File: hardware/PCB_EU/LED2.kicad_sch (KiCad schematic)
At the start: 28 parts, among them J601 LED2 + / GND, J602 BAR2 + / GND, Q601 IRF540ZPBF, U601 LM3429MH/NOPB

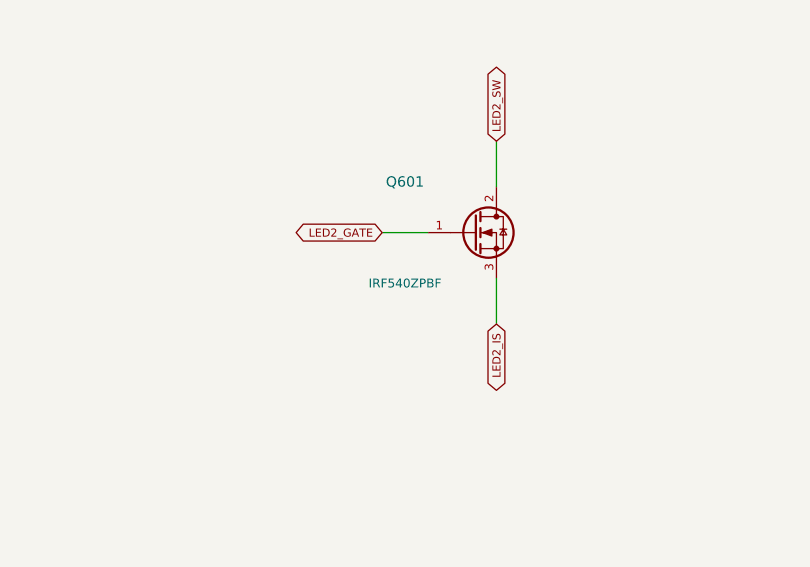
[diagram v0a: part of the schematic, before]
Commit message: PCB_EU: hand-route LED2 power loop, 5 mm cap footprint, TK22E10N1 switches
- C508-C510, C608, C609 (EEUFR1J101LB) use CP_Radial_D8.0mm_P5.00mm, the
  real 5 mm lead pitch; the 3.5 mm footprint is removed and the 3D fit check
  has no known issues left.
- LED2 is placed and routed like LED1: R601 under Q601, D601 anodes toward
  the switch, C611 between C609 leads, wide SW/IS/OUT/GND copper, LED+ and
  the gate on In2. Eight new connected groups are checked.
- route_board.py drops session copper of nets the plan now routes
  (replace_session_nets) and session vias that break hole spacing, and no
  longer prunes GND stitching vias before the pours exist.
- Q501/Q601: IRF540Z -> Toshiba TK22E10N1 (28 nC instead of 42 nC gate
  charge for the 7 V LM3429 driver); BOM 78.59 -> 77.95 EUR.

0 unrouted, DRC 0, schematic parity 0; rebuild is byte-identical.

Co-Authored-By: Claude Opus 5.5 (1M context) <noreply@anthropic.com>
Claude-Session: https://claude.ai/code/session_01AxccZX6Cb4FnRKJMrFYMSX
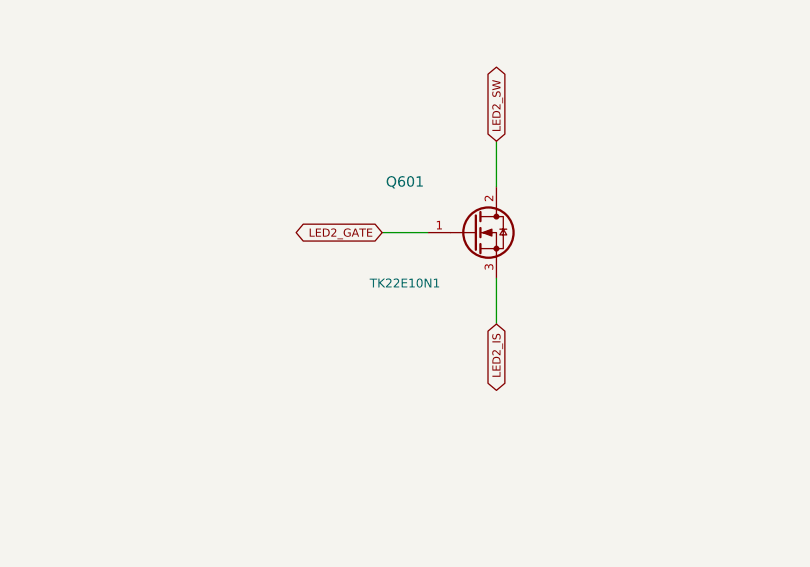
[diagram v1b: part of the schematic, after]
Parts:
- C608, C609: footprint Capacitor_THT:CP_Radial_D8.0mm_P3.50mm -> Capacitor_THT:CP_Radial_D8.0mm_P5.00mm
- Q601: value IRF540ZPBF -> TK22E10N1; MPN IRF540ZPBF -> TK22E10N1
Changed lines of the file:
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@@
 (symbol (lib_id "EU:NMOS") (at 299.72 59.69 0) (unit 1) (in_bom yes) (on_board yes) (dnp no)
 (property "Reference" "Q601" (at 292.1 54.05 0) (effects (font (size 1.15 1.15)) ))
-(property "Value" "IRF540ZPBF" (at 292.1 65.33 0) (effects (font (size 0.98 0.98)) ))
+(property "Value" "TK22E10N1" (at 292.1 65.33 0) (effects (font (size 0.98 0.98)) ))
 (property "Footprint" "Package_TO_SOT_THT:TO-220-3_Vertical" (at 299.72 59.69 0) (effects (font (size 1 1)) (hide yes)))
-(property "Datasheet" "" (at 299.72 59.69 0) (effects (font (size 1 1)) (hide yes)))
-(property "MPN" "IRF540ZPBF" (at 299.72 59.69 0) (effects (font (size 1 1)) (hide yes)))
+(property "Datasheet" "https://docs.rs-online.com/8d7e/0900766b81294f79.pdf" (at 299.72 59.69 0) (effects (font (size 1 1)) (hide yes)))
+(property "MPN" "TK22E10N1" (at 299.72 59.69 0) (effects (font (size 1 1)) (hide yes)))
 (property "Design_note" "Drain tab live. Separate insulated heatsink; exact assembly placement pending" (at 299.72 59.69 0) (effects (font (size 1 1)) (hide yes)))
 (property "FootprintStatus" "PACKAGE ONLY - verify before PCB" (at 299.72 59.69 0) (effects (font (size 1 1)) (hide yes)))
@@
 (property "Reference" "C608" (at 173.99 174.7 0) (effects (font (size 1.15 1.15)) ))
 (property "Value" "100u 63V" (at 173.99 185.98 0) (effects (font (size 0.98 0.98)) ))
-(property "Footprint" "Capacitor_THT:CP_Radial_D8.0mm_P3.50mm" (at 173.99 180.34 0) (effects (font (size 1 1)) (hide yes)))
+(property "Footprint" "Capacitor_THT:CP_Radial_D8.0mm_P5.00mm" (at 173.99 180.34 0) (effects (font (size 1 1)) (hide yes)))
 (property "Datasheet" "" (at 173.99 180.34 0) (effects (font (size 1 1)) (hide yes)))
 (property "MPN" "EEUFR1J101LB" (at 173.99 180.34 0) (effects (font (size 1 1)) (hide yes)))
@@
 (property "Reference" "C609" (at 241.3 174.7 0) (effects (font (size 1.15 1.15)) ))
 (property "Value" "100u 63V" (at 241.3 185.98 0) (effects (font (size 0.98 0.98)) ))
-(property "Footprint" "Capacitor_THT:CP_Radial_D8.0mm_P3.50mm" (at 241.3 180.34 0) (effects (font (size 1 1)) (hide yes)))
+(property "Footprint" "Capacitor_THT:CP_Radial_D8.0mm_P5.00mm" (at 241.3 180.34 0) (effects (font (size 1 1)) (hide yes)))
 (property "Datasheet" "" (at 241.3 180.34 0) (effects (font (size 1 1)) (hide yes)))
 (property "MPN" "EEUFR1J101LB" (at 241.3 180.34 0) (effects (font (size 1 1)) (hide yes)))

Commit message: PCB_EU: all terminals at the board edges, no HS2, fans on KF2510-4A, SHT4x on XH2.54-4P-90
Per Igors (22.10.2026):
- stack stated as 1 oz outer / 0.5 oz inner in DESIGN.md;
- heatsink HS2 removed from the LED2 channel (Q601 runs without a heatsink,
  about 54 C rise, to be measured on the prototype), freed area used for the
  pump terminal J702 and its parts at the right edge;
- J101, J201, J411, J421, J401, J403, J701, J702 moved so that every cable
  entry faces the board edge; J701 changed from DG301R to DG306;
- fan connectors J411/J421 are 4-pin KF2510-4A headers (Molex KK-254
  footprint), J412/J422 removed;
- SHT4x on one right-angle XH2.54-4P-90 header J401 (JST XH S4B-XH-A
  footprint), J402 removed;
- input, trunk and PTC copper re-routed in routing.json; the F101.2 trunk
  now starts with a 2.4 mm neck inside the pad (it was not attached before);
- BOM: quantities and total (82.50 EUR) unchanged, the new rows have no shop
  or price and are flagged for the BOM review.

Checks (KiCad 10.0.7): ERC 0, 56 connectivity checks, 22639 placement checks,
DRC 0 / parity 0 / unconnected 0, rebuild from the repository is byte-identical.
ampacity.py: worst IPC-2221 rise 38 C, three vias above the 2 A rule of thumb.

Co-Authored-By: Claude Sonnet 5.5 <noreply@anthropic.com>
Claude-Session: https://claude.ai/code/session_01AxccZX6Cb4FnRKJMrFYMSX
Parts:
- Q601: Design_note Drain tab live. Separate insulated heatsink; exact assembly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 -> Drain tab live (switch node). No heatsink: ~0.65 W, Rth(ch-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
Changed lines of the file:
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@@
 (property "Datasheet" "https://docs.rs-online.com/8d7e/0900766b81294f79.pdf" (at 299.72 59.69 0) (effects (font (size 1 1)) (hide yes)))
 (property "MPN" "TK22E10N1" (at 299.72 59.69 0) (effects (font (size 1 1)) (hide yes)))
-(property "Design_note" "Drain tab live. Separate insulated heatsink; exact assembly placement pending" (at 299.72 59.69 0) (effects (font (size 1 1)) (hide yes)))
+(property "Design_note" "Drain tab live (switch node). No heatsink: ~0.65 W, Rth(ch-a) 83.3 K/W free air; measure on the prototype" (at 299.72 59.69 0) (effects (font (size 1 1)) (hide yes)))
 (property "FootprintStatus" "PACKAGE ONLY - verify before PCB" (at 299.72 59.69 0) (effects (font (size 1 1)) (hide yes)))
 (pin "1")

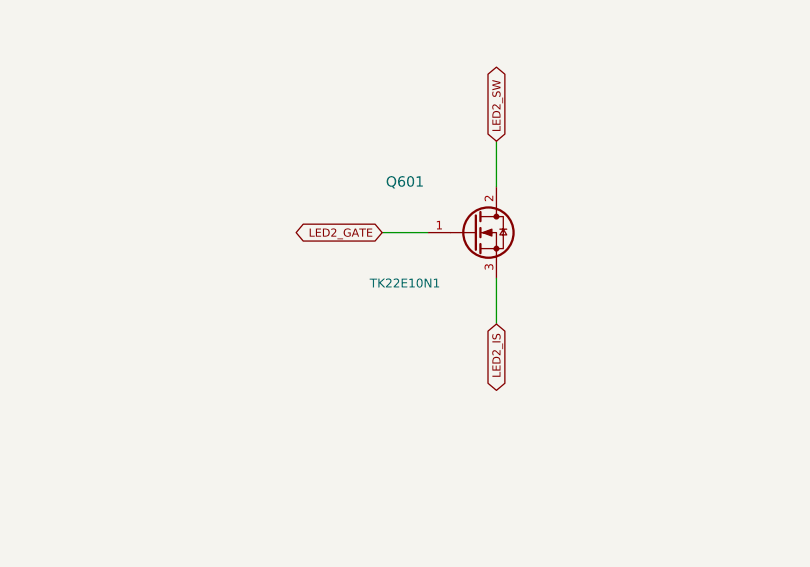
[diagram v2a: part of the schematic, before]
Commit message: PCB_EU: Q601 CSD19534KCS, Q102/Q703 FDB5800, BOM updated
Q601 (LED2 boost switch, no heatsink): TK22E10N1 -> TI CSD19534KCS on the
same TO-220 land. Q102 (reverse polarity) and Q703 (PTC switch):
IRF1010ESPBF -> onsemi FDB5800 on the same TO-263-2 land. Q501 stays
TK22E10N1.

BOM 82.50 -> 85.75 EUR: FDB5800 x2 Salvats 3.96 (was IRF 2.42),
TK22E10N1 x1 instead of x2 (-1.38), CSD19534KCS x1 Electrobase 3.09.
Shipping 5.87 and the two parcels are unchanged.

tools/generate.py rebuilds schematics, design.json and the BOM (the
generator is idempotent). Value/Datasheet/MPN/Design_note of the three
parts are text-patched in PCB_EU.kicad_pcb and review/netlist.xml the way
a KiCad export and build_board.py would write them; review/connectivity.txt
comes from tools/verify.py (56 checks pass). DESIGN.md and README.md are
updated.

KiCad was not run: ERC, DRC, schematic parity and the other KiCad-based
checks of run_checks.py have NOT been run for this commit.

Co-Authored-By: Claude Sonnet 5.5 <noreply@anthropic.com>
Claude-Session: https://claude.ai/code/session_011GxPyRnAFpBjFQ5VURqV5H
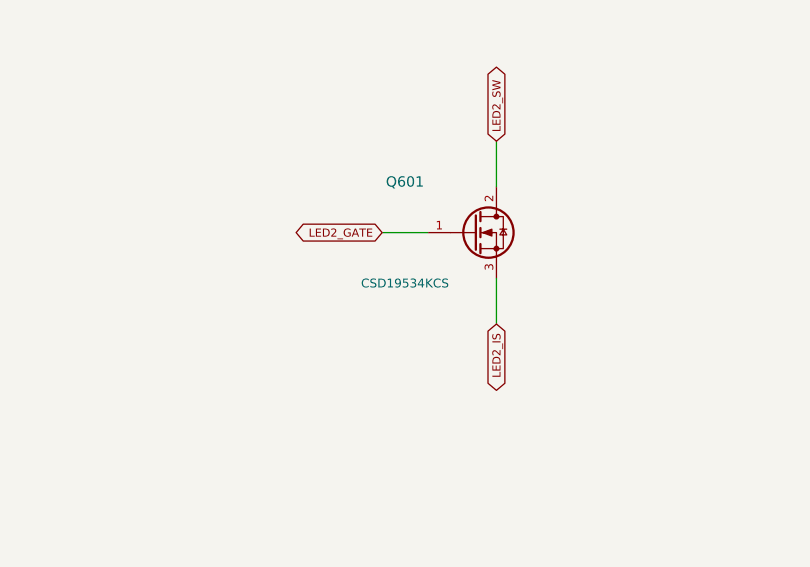
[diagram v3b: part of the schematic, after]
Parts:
- Q601: value TK22E10N1 -> CSD19534KCS; Design_note Drain tab live (switch node). No heatsink: ~0.65 W, Rth(ch-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 -> Drain tab live (switch node). No heatsink: ~0.37 W modelled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; MPN TK22E10N1 -> CSD19534KCS
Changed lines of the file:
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@@
 (symbol (lib_id "EU:NMOS") (at 299.72 59.69 0) (unit 1) (in_bom yes) (on_board yes) (dnp no)
 (property "Reference" "Q601" (at 292.1 54.05 0) (effects (font (size 1.15 1.15)) ))
-(property "Value" "TK22E10N1" (at 292.1 65.33 0) (effects (font (size 0.98 0.98)) ))
+(property "Value" "CSD19534KCS" (at 292.1 65.33 0) (effects (font (size 0.98 0.98)) ))
 (property "Footprint" "Package_TO_SOT_THT:TO-220-3_Vertical" (at 299.72 59.69 0) (effects (font (size 1 1)) (hide yes)))
-(property "Datasheet" "https://docs.rs-online.com/8d7e/0900766b81294f79.pdf" (at 299.72 59.69 0) (effects (font (size 1 1)) (hide yes)))
-(property "MPN" "TK22E10N1" (at 299.72 59.69 0) (effects (font (size 1 1)) (hide yes)))
-(property "Design_note" "Drain tab live (switch node). No heatsink: ~0.65 W, Rth(ch-a) 83.3 K/W free air; measure on the prototype" (at 299.72 59.69 0) (effects (font (size 1 1)) (hide yes)))
+(property "Datasheet" "https://www.ti.com/lit/ds/symlink/csd19534kcs.pdf" (at 299.72 59.69 0) (effects (font (size 1 1)) (hide yes)))
+(property "MPN" "CSD19534KCS" (at 299.72 59.69 0) (effects (font (size 1 1)) (hide yes)))
+(property "Design_note" "Drain tab live (switch node). No heatsink: ~0.37 W modelled, Rth(j-a) 62 K/W free air; measure on the prototype" (at 299.72 59.69 0) (effects (font (size 1 1)) (hide yes)))
 (property "FootprintStatus" "PACKAGE ONLY - verify before PCB" (at 299.72 59.69 0) (effects (font (size 1 1)) (hide yes)))
 (pin "1")
